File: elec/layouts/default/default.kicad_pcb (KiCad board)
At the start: 2 copper layers, 6 parts

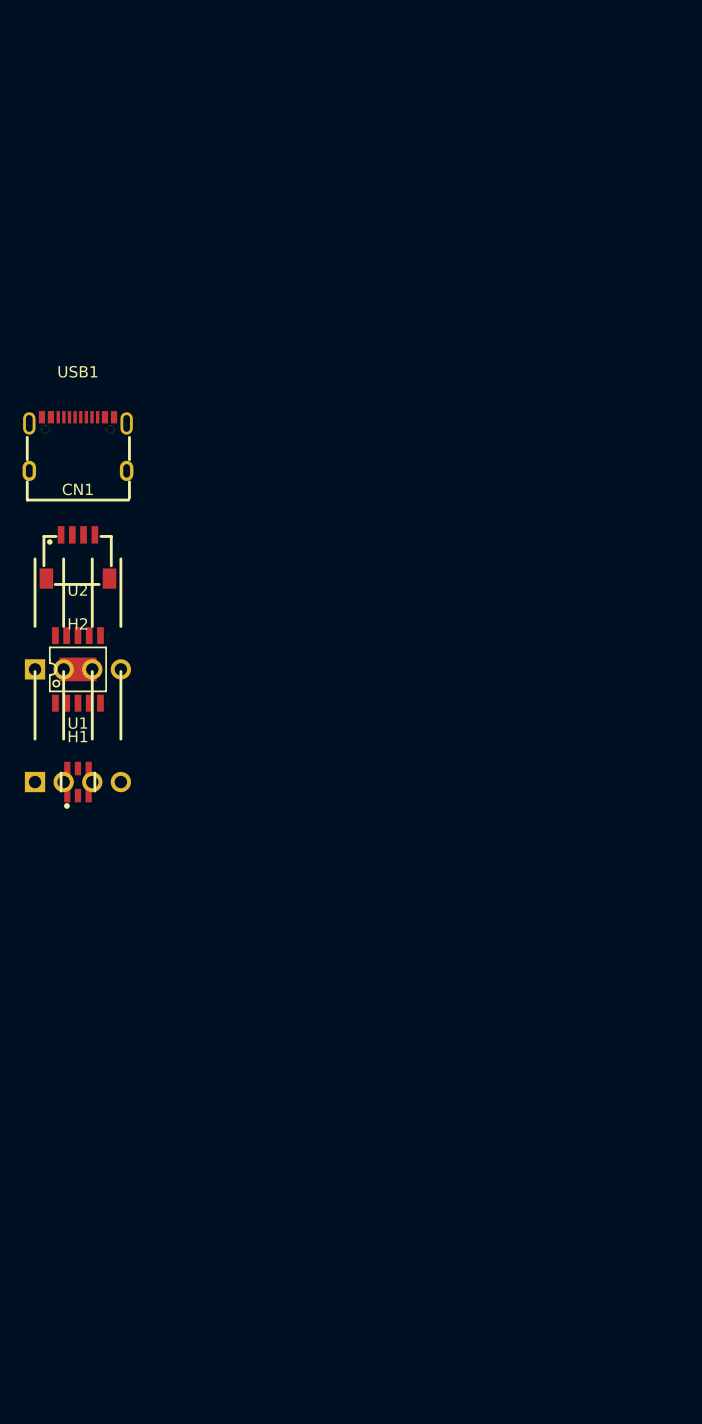
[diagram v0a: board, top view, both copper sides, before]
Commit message: Phase 2: Schematic entry — full circuit connections in Atopile
- Add subsystem modules: usb_pd.ato, buck_5v.ato, fan_driver.ato, sensor_port.ato
- Wire top-level milsblo.ato composing all subsystems with correct net names
- Add named signal aliases (p1–p6) to CJT and JST connector parts to work
  around bare-pin access limitation in atopile v0.12.5
- Auto-picked passive parts committed (resistors, caps, inductor) from ato build
- CH224K VDD zener clamp deferred to Phase 5 (needs interactive ato create part)

ato build passes: 19/19 parts picked, 0 errors
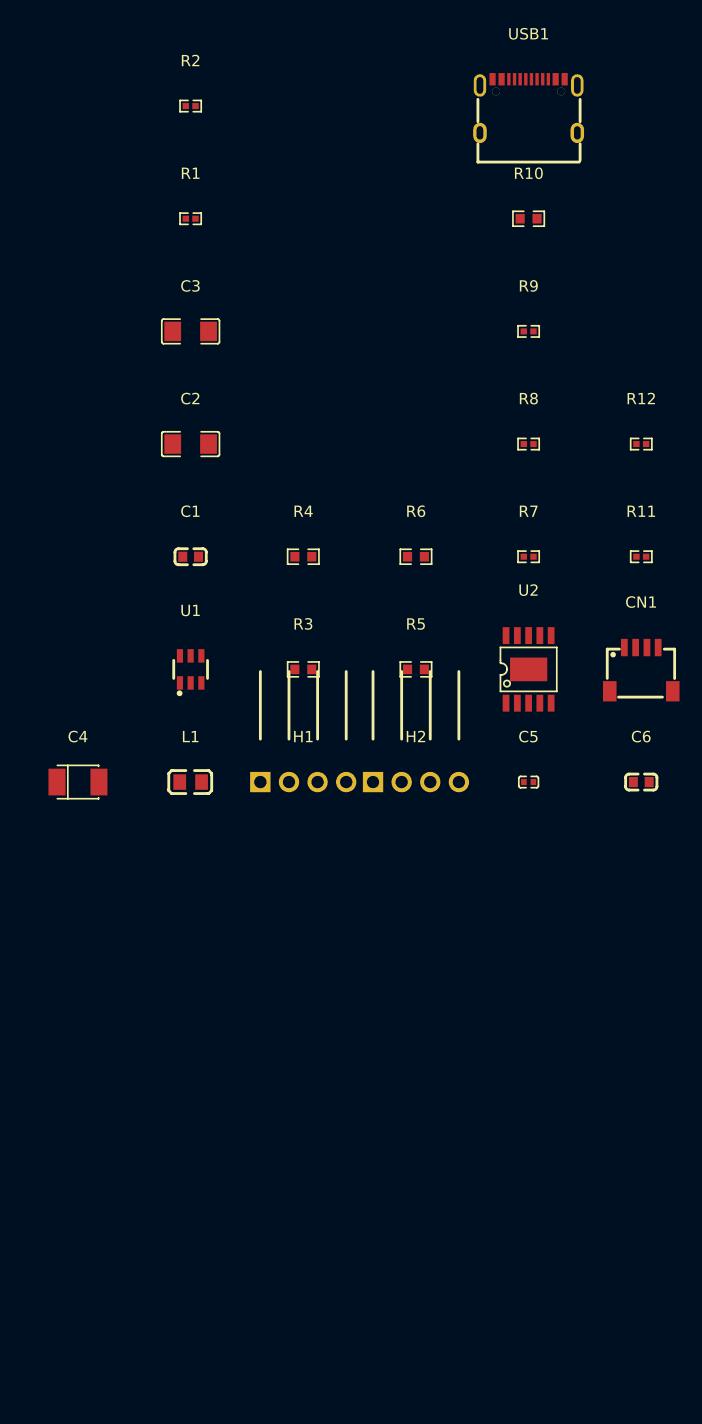
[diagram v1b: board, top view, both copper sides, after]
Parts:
- added C1: 100nF ±10% 50V X7R, YAGEO_CC0603KRX7R9BB104:C0603, F.Cu at (10.0, -20.0)
- added C2: 22µF ±10% 25V X5R, Samsung_Electro_Mechanics_CL31A226KAHNNNE:C1206, F.Cu at (10.0, -30.0)
- added C3: 22µF ±10% 25V X5R, Samsung_Electro_Mechanics_CL31A226KAHNNNE:C1206, F.Cu at (10.0, -40.0)
- added C4: 100µF ±10%, AVX_TAJB107K006RNJ:CASE-B_3528, F.Cu at (0.00, 0.00)
- added C5: 1µF ±10% 25V X5R, Samsung_Electro_Mechanics_CL05A105KA5NQNC:C0402, F.Cu at (40.0, 0.00)
- added C6: 100nF ±10% 50V X7R, YAGEO_CC0603KRX7R9BB104:C0603, F.Cu at (50.0, 0.00)
- added L1: 4.7µH ±10%, FH_CMP201209UD4R7KT:L0805, F.Cu at (10.0, 0.00)
- added R1: 750kΩ ±1% 62.5mW, FOJAN_FRC0402F7503TS:R0402, F.Cu at (10.0, -50.0)
- added R10: 470Ω ±1% 100mW, UNI_ROYAL_0603WAF4700T5E:R0603, F.Cu at (40.0, -50.0)
- added R11: 4.7kΩ ±1% 62.5mW, UNI_ROYAL_0402WGF4701TCE:R0402, F.Cu at (50.0, -20.0)
- added R12: 4.7kΩ ±1% 62.5mW, UNI_ROYAL_0402WGF4701TCE:R0402, F.Cu at (50.0, -30.0)
- added R2: 100kΩ ±1% 62.5mW, UNI_ROYAL_0402WGF1003TCE:R0402, F.Cu at (10.0, -60.0)
- added R3: 100Ω ±1% 100mW, UNI_ROYAL_0603WAF1000T5E:R0603, F.Cu at (20.0, -10.0)
- added R4: 10kΩ ±1% 100mW, UNI_ROYAL_0603WAF1002T5E:R0603, F.Cu at (20.0, -20.0)
- added R5: 100Ω ±1% 100mW, UNI_ROYAL_0603WAF1000T5E:R0603, F.Cu at (30.0, -10.0)
- added R6: 10kΩ ±1% 100mW, UNI_ROYAL_0603WAF1002T5E:R0603, F.Cu at (30.0, -20.0)
- added R7: 5.1kΩ ±1% 62.5mW, UNI_ROYAL_0402WGF5101TCE:R0402, F.Cu at (40.0, -20.0)
- added R8: 5.1kΩ ±1% 62.5mW, UNI_ROYAL_0402WGF5101TCE:R0402, F.Cu at (40.0, -30.0)
- added R9: 24kΩ ±1% 62.5mW, UNI_ROYAL_0402WGF2402TCE:R0402, F.Cu at (40.0, -40.0)
- moved CN1 51.0 mm to (50.0, -10.0)
- moved USB1 50.0 mm to (40.0, -60.0)
- moved U2 40.0 mm to (40.0, -10.0)
- moved H2 31.6 mm to (30.0, 0.00)
- moved H1 20.0 mm to (20.0, 0.00)
- moved U1 14.1 mm to (10.0, -10.0)
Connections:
- CN1 pad 1: footprint-_1 -> gnd
- CN1 pad 2: footprint-_2 -> v3v3
- CN1 pad 3: footprint-_3 -> sda
- CN1 pad 4: footprint-_4 -> scl
- CN1 pad 5: _5 -> gnd
- CN1 pad 6: _6 -> gnd
- H1 pad 1: fan1_header-_1 -> gnd
- H1 pad 2: fan1_header-_2 -> v12
- H1 pad 3: fan1_header-_3 -> fan1-gpio_tach
- H1 pad 4: fan1_header-_4 -> fan1-_4
- H2 pad 1: fan2_header-_1 -> gnd
- H2 pad 2: fan2_header-_2 -> v12
- H2 pad 3: fan2_header-_3 -> fan2-gpio_tach
- H2 pad 4: fan2_header-_4 -> fan2-_4
- U1 pad 2: EN -> pg
- U1 pad 3: VIN -> v12
- U1 pad 4: buck-GND -> gnd
- U2 pad 10: PG -> pg
- U2 pad 11: footprint-GND-0 -> gnd
- U2 pad 6: footprint-CC2-0 -> CC2
- U2 pad 7: footprint-CC1-0 -> CC1
- U2 pad 8: footprint-VBUS-0 -> v12
- USB1 pad 1: footprint-GND-1 -> gnd
- USB1 pad 10: footprint-CC2-1 -> CC2
- USB1 pad 11: footprint-VBUS-1 -> v12
- USB1 pad 12: footprint-GND-1 -> gnd
- USB1 pad 13: SHELL -> gnd
- USB1 pad 14: SHELL -> gnd
- USB1 pad 2: footprint-VBUS-1 -> v12
- USB1 pad 4: footprint-CC1-1 -> CC1
- USB1 pad 6: DP1 -> DP
- USB1 pad 7: DN1 -> DM

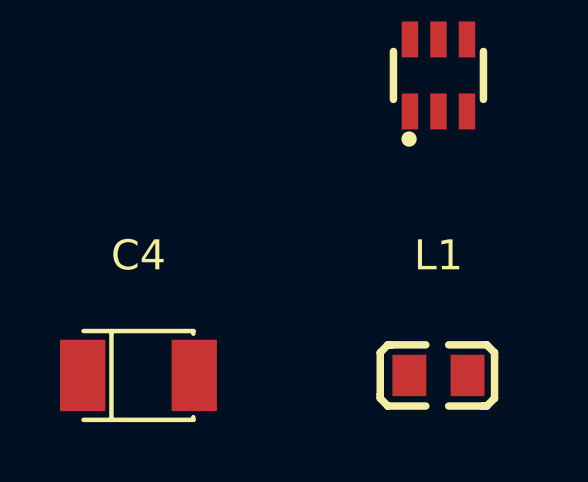
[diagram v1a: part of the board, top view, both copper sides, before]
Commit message: Phase 4: Breadboard prototype — firmware, test guide, Zener fix
Add BZT52C5V1 (LCSC C173407) 5.1V Zener clamp to usb_pd.ato to protect
CH224K VDD pin from 12V VBUS after PD negotiation (was unprotected; IC
would be destroyed without it). Add ESPHome firmware config and
breadboard test guide with 6-stage test sequence.

- elec/src/power/usb_pd.ato: add z_vdd Zener clamp (C→VDD, A→GND)
- elec/src/parts/MDD_Microdiode_Electronics_BZT52C5V1/: new Zener part
- firmware/milsblo.yaml: ESPHome config (25kHz PWM, tach, BME280, PG)
- firmware/secrets.yaml: secrets template
- docs/breadboard-test.md: 6-stage test sequence with safety warnings
- CLAUDE.md: add Zener to architecture table, update Phase 2 USB-PD spec
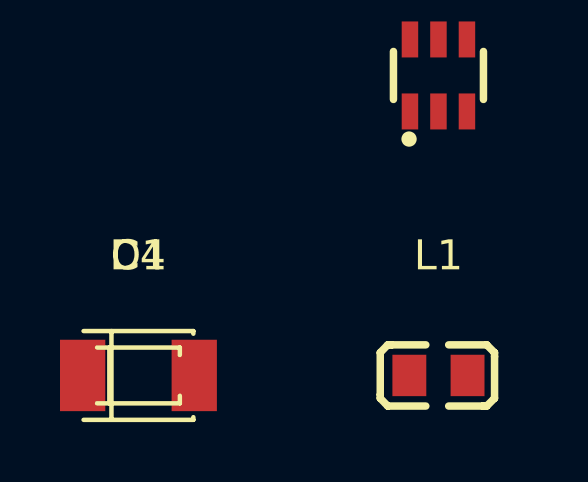
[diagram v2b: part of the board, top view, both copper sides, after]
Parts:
- added D1: , MDD_Microdiode_Electronics_BZT52C5V1:SOD-123_L2.7-W1.6-LS3.7-RD, F.Cu at (0.00, 0.00)
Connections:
- net VDD renamed C
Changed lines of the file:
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@@
     (net 60 "DN2")
     (net 61 "fan2-gpio_tach")
-    (net 62 "VDD")
     (net 63 "scl")
     (net 64 "SBU1")
@@
     (net 71 "SW")
     (net 72 "CFG1")
+    (net 1 "C")
     (footprint "AVX_TAJB107K006RNJ:CASE-B_3528"
         (layer "F.Cu")
@@
             (size 0.5 0.54)
             (layers "F.Cu" "F.Paste" "F.Mask")
-            (net 62 "VDD")
+            (net 1 "C")
         )
         (model "${KIPRJMOD}/../../src/parts/Samsung_Electro_Mechanics_CL05A105KA5NQNC/C0402_L1.0-W0.5-H0.5.step"
@@
             (size 1.5 0.6)
             (layers "F.Cu" "F.Paste" "F.Mask")
-            (net 62 "VDD")
+            (net 1 "C")
         )
         (pad "11" smd rect
@@
             (size 0.81 0.86)
             (layers "F.Cu" "F.Paste" "F.Mask")
-            (net 62 "VDD")
+            (net 1 "C")
         )
         (pad "1" smd rect
@@
             )
         )
+    )
+    (footprint "MDD_Microdiode_Electronics_BZT52C5V1:SOD-123_L2.7-W1.6-LS3.7-RD"
+        (layer "F.Cu")
+        (at 0 0 0)
+        (property "Reference" "D1"
+            (at 0 -4 0)
+            (layer "F.SilkS")
+            (hide no)
+            (effects
+                (font
+                    (size 1 1)
+                    (thickness 0.15)
+                )
+            )
+        )
+        (property "Value" ""
+            (at 0 4 0)
+            (layer "F.Fab")
+            (hide no)
+            (effects
+                (font
+                    (size 1 1)
+                    (thickness 0.15)
+                )
+            )
+        )
+        (property "checksum" "b050ba68dab654d46030f5bab1f4232b7049a2132be2a127ef80fb73816e5a12"
+            (at 0 0 0)
+            (layer "User.9")
+            (hide no)
+            (effects
+                (font
+                    (size 0.125 0.125)
+                    (thickness 0.01875)
+                )
+                (hide yes)
+            )
+        )
+        (property "__atopile_lib_fp_hash__" "630451bc-0986-da2d-1050-7e110f879a15"
+            (at 0 0 0)
+            (layer "User.9")
+            (hide yes)
+            (effects
+                (font
+                    (size 0.125 0.125)
+                    (thickness 0.01875)
+                )
+            )
+        )
+        (property "LCSC" "C173407"
+            (at 0 0 0)
+            (layer "User.9")
+            (hide yes)
+            (effects
+                (font
+                    (size 0.125 0.125)
+                    (thickness 0.01875)
+                )
+            )
+        )
+        (property "Manufacturer" "MDD（Microdiode Electronics）"
+            (at 0 0 0)
+            (layer "User.9")
+            (hide yes)
+            (effects
+                (font
+                    (size 0.125 0.125)
+                    (thickness 0.01875)
+                )
+            )
+        )
+        (property "Partnumber" "BZT52C5V1"
+            (at 0 0 0)
+            (layer "User.9")
+            (hide yes)
+            (effects
+                (font
+                    (size 0.125 0.125)
+                    (thickness 0.01875)
+                )
+            )
+        )
+        (property "atopile_address" "pd.z_vdd"
+            (at 0 0 0)
+            (layer "User.9")
+            (hide yes)
+            (effects
+                (font
+                    (size 0.125 0.125)
+                    (thickness 0.01875)
+                )
+            )
+        )
+        (attr smd)
+        (fp_line
+            (start -1.38 -0.93)
+            (end 1.38 -0.93)
+            (stroke
+                (width 0.15)
+                (type solid)
+            )
+            (layer "F.SilkS")
+        )
+        (fp_line
+            (start 1.38 -0.93)
+            (end 1.38 -0.68)
+            (stroke
+                (width 0.15)
+                (type solid)
+            )
+            (layer "F.SilkS")
+        )
+        (fp_line
+            (start -1.38 0.93)
+            (end 1.38 0.93)
+            (stroke
+                (width 0.15)
+                (type solid)
+            )
+            (layer "F.SilkS")
+        )
+        (fp_line
+            (start 1.38 0.93)
+            (end 1.38 0.68)
+            (stroke
+                (width 0.15)
+                (type solid)
+            )
+            (layer "F.SilkS")
+        )
+        (fp_line
+            (start -0.97 -0.93)
+            (end -0.97 0.93)
+            (stroke
+                (width 0.15)
+                (type solid)
+            )
+            (layer "F.SilkS")
+        )
+        (fp_circle
+            (center -1.85 0.8)
+            (end -1.82 0.8)
+            (stroke
+                (width 0.06)
+                (type solid)
+            )
+            (fill no)
+            (layer "F.Fab")
+        )
+        (fp_text user "%R"
+            (at 0 0 0)
+            (layer "F.Fab")
+            (effects
+                (font
+                    (size 1 1)
+                    (thickness 0.15)
+                )
+            )
+            (unlocked no)
+        )
+        (fp_text user "${REFERENCE}"
+            (at 0 -4 0)
+            (layer "F.SilkS")
+            (effects
+                (font
+                    (size 1 1)
+                    (thickness 0.15)
+                )
+            )
+            (unlocked no)
+        )
+        (pad "2" smd rect
+            (at 1.64 0 0)
+            (size 0.91 1.22)
+            (layers "F.Cu" "F.Paste" "F.Mask")
+            (net 58 "gnd")
+        )
+        (pad "1" smd rect
+            (at -1.64 0 0)
+            (size 0.91 1.22)
+            (layers "F.Cu" "F.Paste" "F.Mask")
+            (net 1 "C")
+        )
+        (model "${KIPRJMOD}/../../src/parts/MDD_Microdiode_Electronics_BZT52C5V1/SOD-123_L2.7-W1.6-LS3.7-RD-2.step"
+            (offset
+                (xyz 0 0 0)
+            )
+            (scale
+                (xyz 1 1 1)
+            )
+            (rotate
+                (xyz 0 0 180)
+            )
+        )
